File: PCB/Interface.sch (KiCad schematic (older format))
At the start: 12 parts, among them U5 USBLC6-2SC6

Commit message: Schema: add mcu, RGB LED signalization, reset circuit
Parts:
- removed J?: USB_B, Connector_USB:USB_B_OST_USB-B1HSxx_Horizontal, symbol Connector:USB_B
- removed R? (x2): 22R, Resistor_SMD:R_0603_1608Metric, symbol Device:R
- added J?: USB_B, Connector_USB:USB_B_OST_USB-B1HSxx_Horizontal, symbol Connector:USB_B
- added R? (x2): 22R, Resistor_SMD:R_0603_1608Metric, symbol Device:R
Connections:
- net D+: now also R?.2
- net D-: now also R?.2
- net GND: now also J?.4 (GND)
- net USB+: now also J?.3 (D+)
- net USB-: now also J?.2 (D-)
- net USB_D+: now also R?.1
- net USB_D-: now also R?.1
- net USB_VCC: now also J?.1 (VBUS)
- net at L?.1: now also J?.5 (Shield)
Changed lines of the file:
@@
 $Comp
 L Connector:USB_B J?
-U 1 1 5BDB25CF
+U 1 1 5E44C3FC
 P 1850 2400
 F 0 "J?" H 1905 2867 50  0000 C CNN
@@
 $Comp
 L power:GND #PWR?
-U 1 1 5BDB637A
+U 1 1 5E44C3FD
 P 1850 3200
 F 0 "#PWR?" H 1850 2950 50  0001 C CNN
@@
 $Comp
 L Device:R R?
-U 1 1 5BDB6C04
+U 1 1 5E44C3FF
 P 4050 2500
 F 0 "R?" V 4250 2500 50  0000 C CNN
@@
 $Comp
 L Device:R R?
-U 1 1 5BDB6B35
+U 1 1 5E44C3FE
 P 4050 2300
 F 0 "R?" V 3843 2300 50  0000 C CNN
@@
 $Comp
 L power:+5V #PWR?
-U 1 1 5DA7C335
+U 1 1 5E44C400
 P 2400 4800
 F 0 "#PWR?" H 2400 4650 50  0001 C CNN
@@
 $Comp
 L power:GND #PWR?
-U 1 1 5DA7D06F
+U 1 1 5E44C401
 P 2400 4650
 F 0 "#PWR?" H 2400 4400 50  0001 C CNN

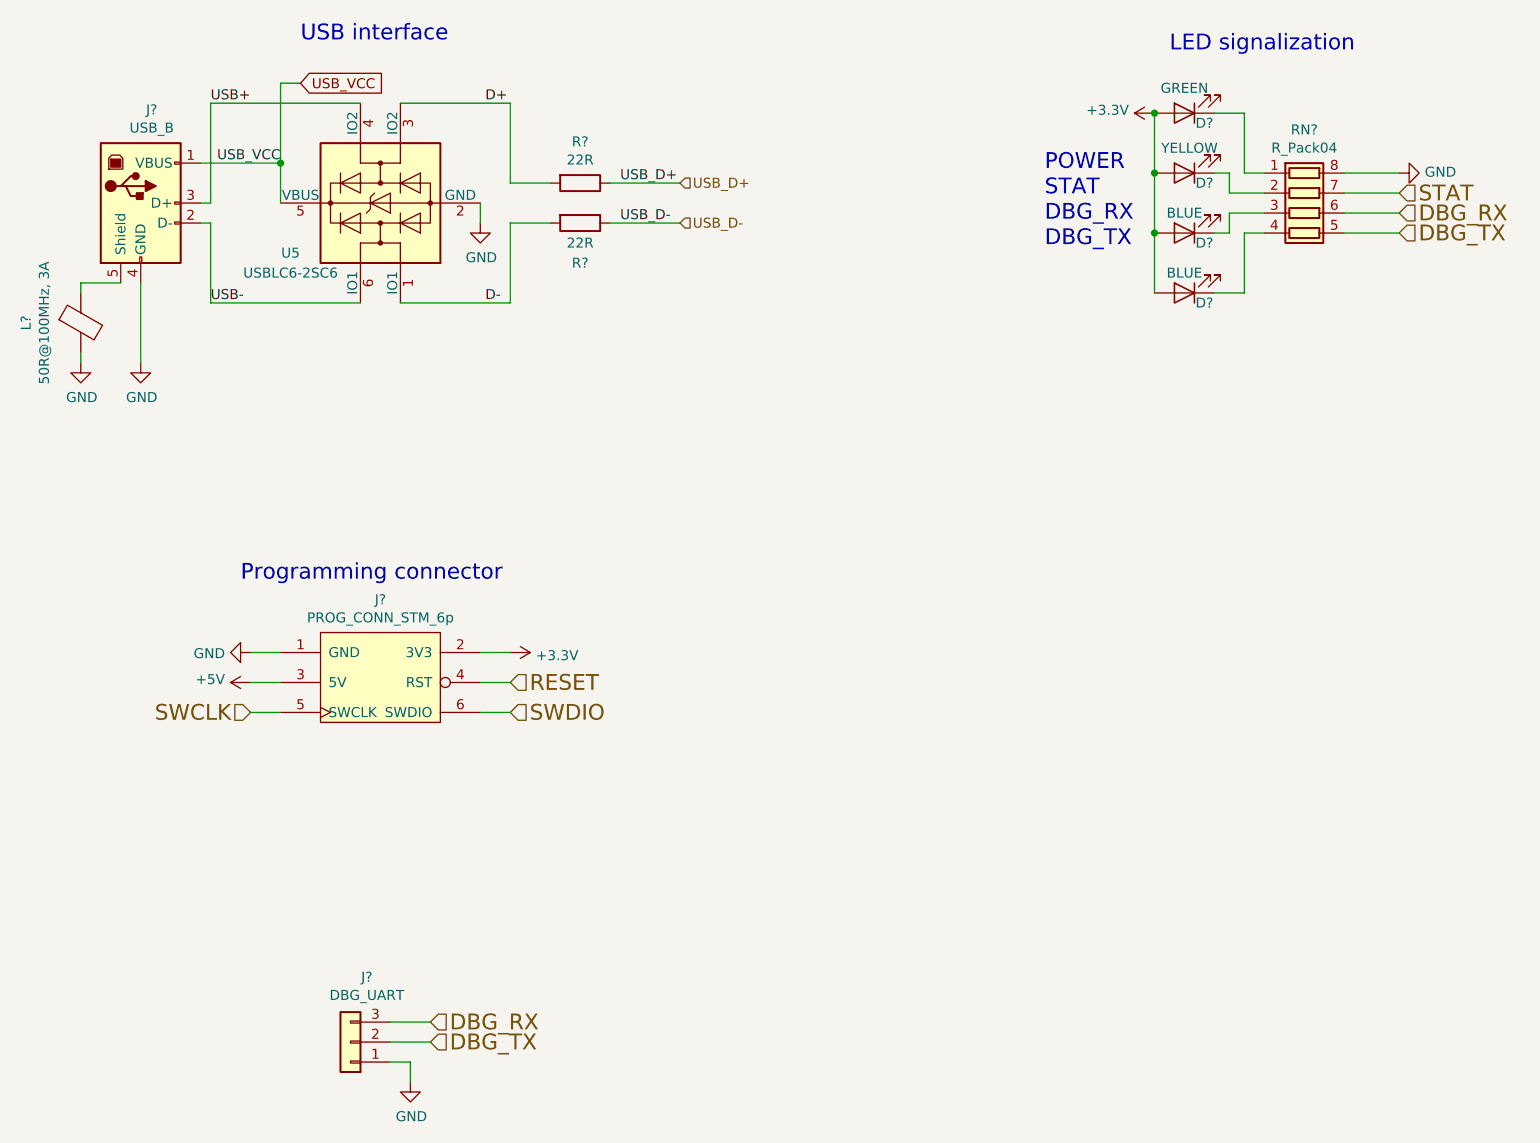
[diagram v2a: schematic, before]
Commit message: Schema: new part annotation, package assignment
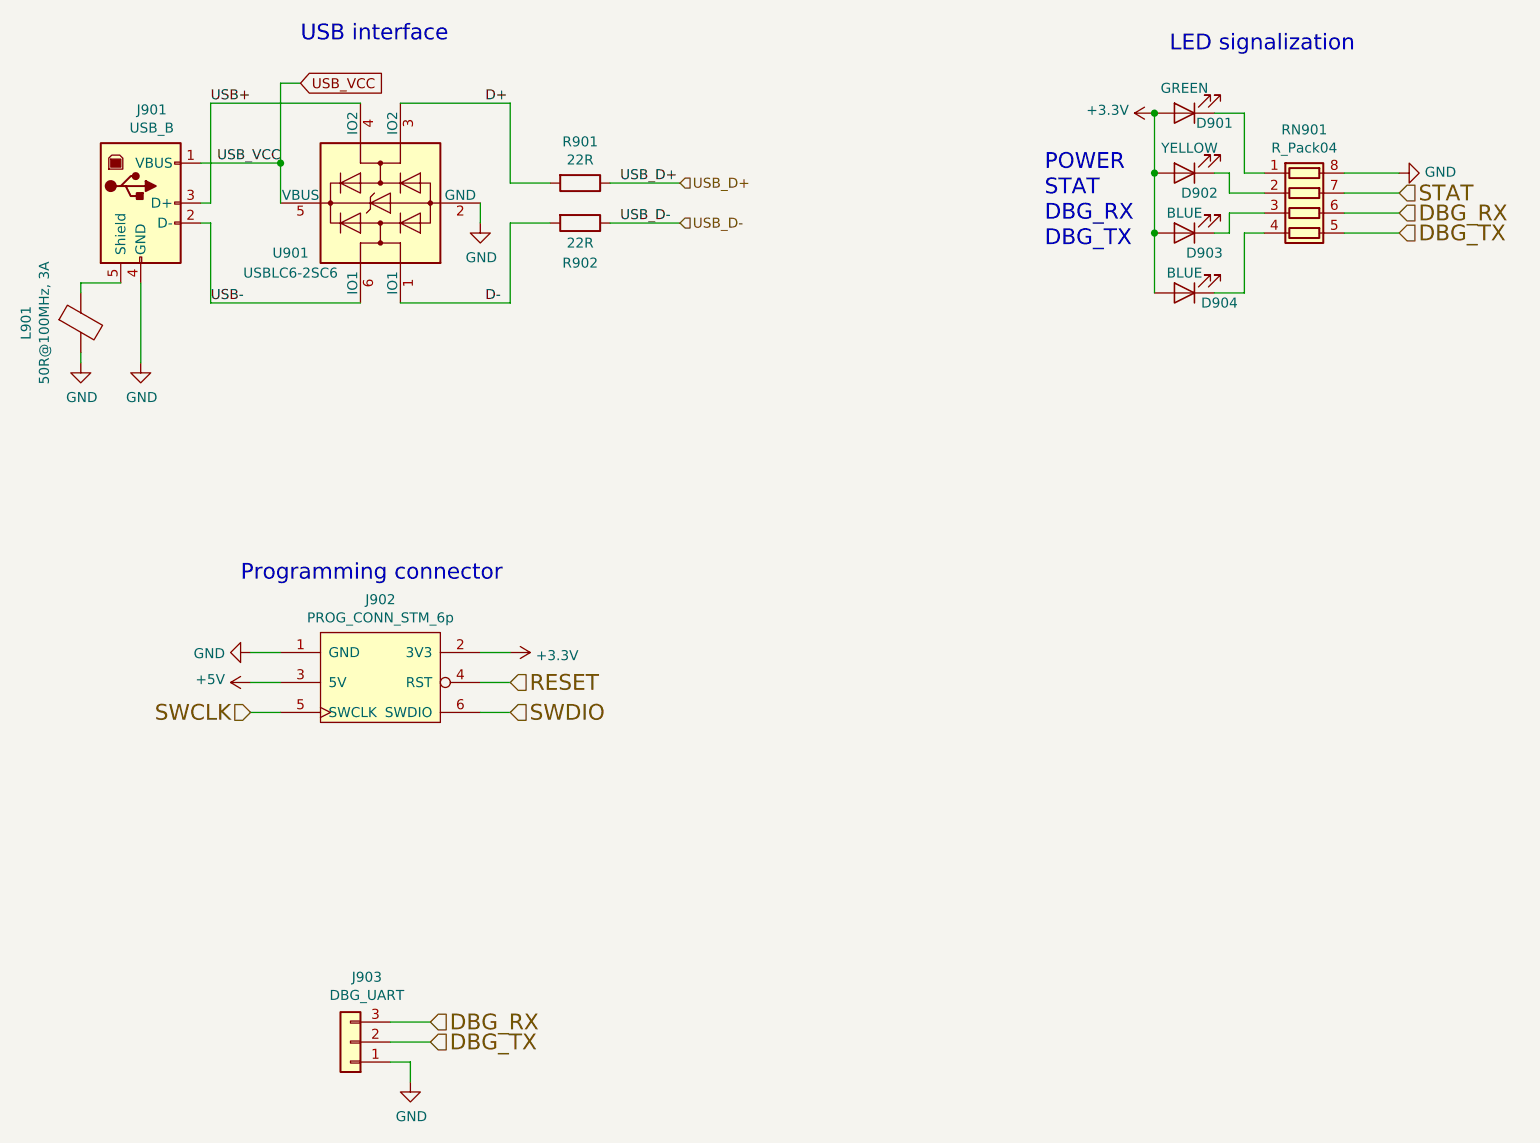
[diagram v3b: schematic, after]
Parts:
- gave numbers to parts that had none: 11
- renumbered U5 to U901
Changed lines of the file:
@@
 USB_VCC
 $Comp
-L Connector:USB_B J?
+L Connector:USB_B J901
 U 1 1 5E44C3FC
 P 1850 2400
-F 0 "J?" H 1905 2867 50  0000 C CNN
+F 0 "J901" H 1905 2867 50  0000 C CNN
 F 1 "USB_B" H 1905 2776 50  0000 C CNN
 F 2 "Connector_USB:USB_B_OST_USB-B1HSxx_Horizontal" H 2000 2350 50  0001 C CNN
@@
 $EndComp
 $Comp
-L power:GND #PWR?
+L power:GND #PWR0905
 U 1 1 5E44C3FD
 P 1850 3200
-F 0 "#PWR?" H 1850 2950 50  0001 C CNN
+F 0 "#PWR0905" H 1850 2950 50  0001 C CNN
 F 1 "GND" H 1855 3027 50  0000 C CNN
 F 2 "" H 1850 3200 50  0001 C CNN
@@
 $EndComp
 $Comp
-L Device:Ferrite_Bead L?
+L Device:Ferrite_Bead L901
 U 1 1 5E442BE2
 P 1550 3000
-F 0 "L?" V 1276 3000 50  0000 C CNN
+F 0 "L901" V 1276 3000 50  0000 C CNN
 F 1 "50R@100MHz, 3A" V 1367 3000 50  0000 C CNN
 F 2 "Inductor_SMD:L_1206_3216Metric" V 1480 3000 50  0001 C CNN
@@
 	1550 2800 1550 2850
 $Comp
-L power:GND #PWR?
+L power:GND #PWR0904
 U 1 1 5E442BE3
 P 1550 3200
-F 0 "#PWR?" H 1550 2950 50  0001 C CNN
+F 0 "#PWR0904" H 1550 2950 50  0001 C CNN
 F 1 "GND" H 1555 3027 50  0000 C CNN
 F 2 "" H 1550 3200 50  0001 C CNN
@@
 	2550 2400 2550 2200
 $Comp
-L power:GND #PWR?
+L power:GND #PWR0903
 U 1 1 5E442BE4
 P 3550 2500
-F 0 "#PWR?" H 3550 2250 50  0001 C CNN
+F 0 "#PWR0903" H 3550 2250 50  0001 C CNN
 F 1 "GND" H 3555 2327 50  0000 C CNN
 F 2 "" H 3550 2500 50  0001 C CNN
@@
 	3700 2300 3900 2300
 $Comp
-L Device:R R?
+L Device:R R902
 U 1 1 5E44C3FF
 P 4050 2500
-F 0 "R?" V 4250 2500 50  0000 C CNN
+F 0 "R902" V 4250 2500 50  0000 C CNN
 F 1 "22R" V 4150 2500 50  0000 C CNN
 F 2 "Resistor_SMD:R_0603_1608Metric" V 3980 2500 50  0001 C CNN
@@
 $EndComp
 $Comp
-L Device:R R?
+L Device:R R901
 U 1 1 5E44C3FE
 P 4050 2300
-F 0 "R?" V 3843 2300 50  0000 C CNN
+F 0 "R901" V 3843 2300 50  0000 C CNN
 F 1 "22R" V 3934 2300 50  0000 C CNN
 F 2 "Resistor_SMD:R_0603_1608Metric" V 3980 2300 50  0001 C CNN
@@
 $EndComp
 $Comp
-L vrasseo-rescue:USBLC6-2SC6-Power_Protection U5
+L vrasseo-rescue:USBLC6-2SC6-Power_Protection U?
 U 1 1 5E442BDD
 P 3050 2400
-AR Path="/5E442BDD" Ref="U5"  Part="1"
-AR Path="/5BA4084F/5E442BDD" Ref="U5"  Part="1"
-AR Path="/5DA29F03/5E442BDD" Ref="U5"  Part="1"
-AR Path="/5E43C48F/5E442BDD" Ref="U?"  Part="1"
-F 0 "U?" V 2800 2850 50  0000 C CNN
+AR Path="/5E442BDD" Ref="U?"  Part="1"
+AR Path="/5BA4084F/5E442BDD" Ref="U?"  Part="1"
+AR Path="/5DA29F03/5E442BDD" Ref="U?"  Part="1"
+AR Path="/5E43C48F/5E442BDD" Ref="U901"  Part="1"
+F 0 "U901" V 2800 2850 50  0000 C CNN
 F 1 "USBLC6-2SC6" V 2700 2850 50  0000 C CNN
 F 2 "Package_TO_SOT_SMD:SOT-23-6" H 2300 2800 50  0001 C CNN
@@
 	2550 1800 2550 2200
 $Comp
-L TCY_connectors:PROG_CONN_STM_6p J?
+L TCY_connectors:PROG_CONN_STM_6p J902
 U 1 1 5E442BE5
 P 3050 4800
-F 0 "J?" H 3050 5215 50  0000 C CNN
+F 0 "J902" H 3050 5215 50  0000 C CNN
 F 1 "PROG_CONN_STM_6p" H 3050 5124 50  0000 C CNN
 F 2 "Connector_IDC:IDC-Header_2x03_P2.54mm_Horizontal" H 2850 5200 50  0001 C CNN
@@
 SWCLK
 $Comp
-L power:+5V #PWR?
+L power:+5V #PWR0908
 U 1 1 5E44C400
 P 2400 4800
-F 0 "#PWR?" H 2400 4650 50  0001 C CNN
+F 0 "#PWR0908" H 2400 4650 50  0001 C CNN
 F 1 "+5V" V 2415 4928 50  0000 L CNN
 F 2 "" H 2400 4800 50  0001 C CNN
@@
 $EndComp
 $Comp
-L power:+3.3V #PWR?
+L power:+3.3V #PWR0907
 U 1 1 5E442BE7
 P 3700 4650
-F 0 "#PWR?" H 3700 4500 50  0001 C CNN
+F 0 "#PWR0907" H 3700 4500 50  0001 C CNN
 F 1 "+3.3V" V 3715 4778 50  0000 L CNN
 F 2 "" H 3700 4650 50  0001 C CNN
@@
 $EndComp
 $Comp
-L power:GND #PWR?
+L power:GND #PWR0906
 U 1 1 5E44C401
 P 2400 4650
-F 0 "#PWR?" H 2400 4400 50  0001 C CNN
+F 0 "#PWR0906" H 2400 4400 50  0001 C CNN
 F 1 "GND" V 2405 4522 50  0000 R CNN
 F 2 "" H 2400 4650 50  0001 C CNN
@@
 Programming connector
 $Comp
-L Connector_Generic:Conn_01x03 J?
+L Connector_Generic:Conn_01x03 J903
 U 1 1 5E442BE9
 P 2900 6600
-F 0 "J?" H 2818 6275 50  0000 C CNN
+F 0 "J903" H 2818 6275 50  0000 C CNN
 F 1 "DBG_UART" H 2818 6366 50  0000 C CNN
 F 2 "Connector_PinHeader_2.54mm:PinHeader_1x03_P2.54mm_Vertical" H 2900 6600 50  0001 C CNN
@@
 	3200 6700 3200 6800
 $Comp
-L power:GND #PWR?
+L power:GND #PWR0909
 U 1 1 5E442BEA
 P 3200 6800
-F 0 "#PWR?" H 3200 6550 50  0001 C CNN
+F 0 "#PWR0909" H 3200 6550 50  0001 C CNN
 F 1 "GND" H 3205 6627 50  0000 C CNN
 F 2 "" H 3200 6800 50  0001 C CNN
@@
 DBG_TX
 $Comp
-L Device:R_Pack04 RN?
+L Device:R_Pack04 RN901
 U 1 1 5E442BEB
 P 7675 2450
-F 0 "RN?" V 7258 2450 50  0000 C CNN
+F 0 "RN901" V 7258 2450 50  0000 C CNN
 F 1 "R_Pack04" V 7349 2450 50  0000 C CNN
 F 2 "Resistor_SMD:R_Array_Convex_4x0603" V 7950 2450 50  0001 C CNN
@@
 $EndComp
 $Comp
-L Device:LED D?
+L Device:LED D902
 U 1 1 5E442BEC
 P 7075 2250
-F 0 "D?" H 6975 2300 50  0000 C CNN
+F 0 "D902" H 7000 2350 50  0000 C CNN
 F 1 "YELLOW" H 7050 2125 50  0000 C CNN
 F 2 "LED_SMD:LED_0603_1608Metric_Castellated" H 7075 2250 50  0001 C CNN
@@
 $EndComp
 $Comp
-L Device:LED D?
+L Device:LED D903
 U 1 1 5E442BED
 P 7075 2550
-F 0 "D?" H 6975 2600 50  0000 C CNN
+F 0 "D903" H 6975 2650 50  0000 C CNN
 F 1 "BLUE" H 7075 2450 50  0000 C CNN
 F 2 "LED_SMD:LED_0603_1608Metric_Castellated" H 7075 2550 50  0001 C CNN
@@
 $EndComp
 $Comp
-L Device:LED D?
+L Device:LED D904
 U 1 1 5E442BEE
 P 7075 2850
-F 0 "D?" H 6975 2900 50  0000 C CNN
+F 0 "D904" H 6900 2900 50  0000 C CNN
 F 1 "BLUE" H 7075 2750 50  0000 C CNN
 F 2 "LED_SMD:LED_0603_1608Metric_Castellated" H 7075 2850 50  0001 C CNN
@@
 $EndComp
 $Comp
-L Device:LED D?
+L Device:LED D901
 U 1 1 5E442BEF
 P 7075 1950
-F 0 "D?" H 6975 2000 50  0000 C CNN
+F 0 "D901" H 6925 2000 50  0000 C CNN
 F 1 "GREEN" H 7075 1825 50  0000 C CNN
 F 2 "LED_SMD:LED_0603_1608Metric_Castellated" H 7075 1950 50  0001 C CNN
@@
 Connection ~ 6925 1950
 $Comp
-L power:+3.3V #PWR?
+L power:+3.3V #PWR0901
 U 1 1 5DAA918B
 P 6925 1950
-F 0 "#PWR?" H 6925 1800 50  0001 C CNN
+F 0 "#PWR0901" H 6925 1800 50  0001 C CNN
 F 1 "+3.3V" V 6940 2078 50  0000 L CNN
 F 2 "" H 6925 1950 50  0001 C CNN
@@
 LED signalization
 $Comp
-L power:GND #PWR?
+L power:GND #PWR0902
 U 1 1 5DAC4CBF
 P 8150 2250
-F 0 "#PWR?" H 8150 2000 50  0001 C CNN
+F 0 "#PWR0902" H 8150 2000 50  0001 C CNN
 F 1 "GND" V 8155 2122 50  0000 R CNN
 F 2 "" H 8150 2250 50  0001 C CNN

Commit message: PCB: change programing and debugging IDC connectors to vertical version
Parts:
- J902: footprint Connector_IDC:IDC-Header_2x03_P2.54mm_Horizontal -> Connector_IDC:IDC-Header_2x03_P2.54mm_Vertical
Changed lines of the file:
@@
 F 0 "J902" H 3050 5215 50  0000 C CNN
 F 1 "PROG_CONN_STM_6p" H 3050 5124 50  0000 C CNN
-F 2 "Connector_IDC:IDC-Header_2x03_P2.54mm_Horizontal" H 2850 5200 50  0001 C CNN
+F 2 "Connector_IDC:IDC-Header_2x03_P2.54mm_Vertical" H 2850 5200 50  0001 C CNN
 F 3 "" H 2850 5200 50  0001 C CNN
 	1    3050 4800

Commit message: PCB: change package size of USB ferrite from 1206 to 0803
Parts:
- L901: footprint Inductor_SMD:L_1206_3216Metric -> Inductor_SMD:L_0805_2012Metric
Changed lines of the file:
@@
 F 0 "L901" V 1276 3000 50  0000 C CNN
 F 1 "50R@100MHz, 3A" V 1367 3000 50  0000 C CNN
-F 2 "Inductor_SMD:L_1206_3216Metric" V 1480 3000 50  0001 C CNN
+F 2 "Inductor_SMD:L_0805_2012Metric" V 1480 3000 50  0001 C CNN
 F 3 "~" H 1550 3000 50  0001 C CNN
 	1    1550 3000

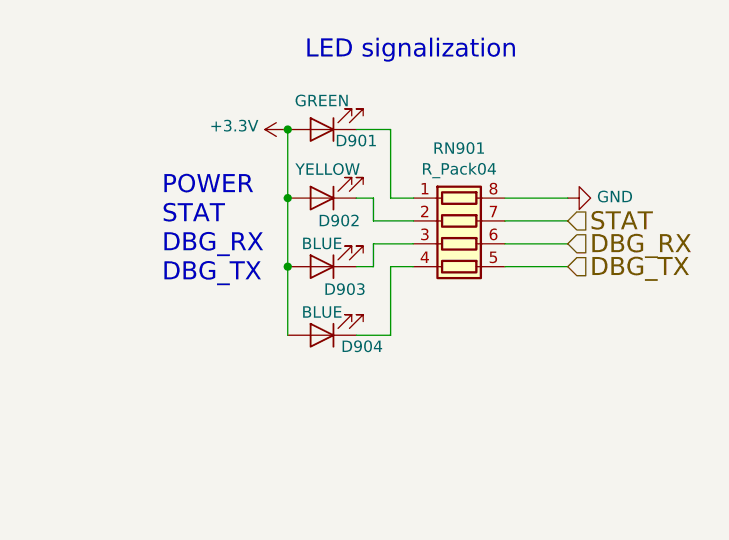
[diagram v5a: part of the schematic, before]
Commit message: Schema & PCB: add routing of MCu connection, debug and extension port
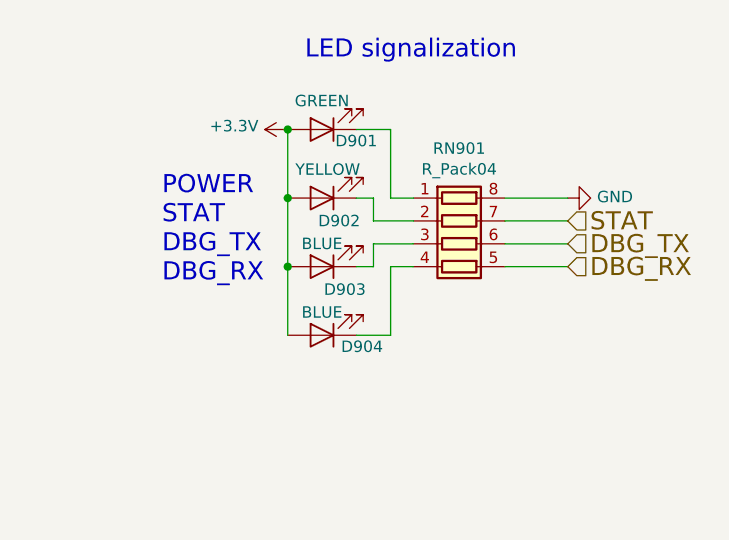
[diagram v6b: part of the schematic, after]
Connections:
- net DBG_RX: now also RN901.5 (R4.2); no longer RN901.6 (R3.2)
- net DBG_TX: now also RN901.6 (R3.2); no longer RN901.5 (R4.2)
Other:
- note added: "POWER\nSTAT\nDBG_TX\nDBG_RX"
- note removed: "POWER\nSTAT\nDBG_RX\nDBG_TX"
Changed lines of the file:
@@
 Wire Wire Line
 	7875 2450 8150 2450
+Text HLabel 8150 2550 2    79   Input ~ 0
+DBG_RX
 Text HLabel 8150 2450 2    79   Input ~ 0
-DBG_RX
-Text HLabel 8150 2550 2    79   Input ~ 0
 DBG_TX
 Text Notes 7000 1650 0    79   ~ 0
@@
 D-
 Text Notes 6375 2625 0    79   ~ 0
-POWER\nSTAT\nDBG_RX\nDBG_TX
+POWER\nSTAT\nDBG_TX\nDBG_RX
 $EndSCHEMATC
